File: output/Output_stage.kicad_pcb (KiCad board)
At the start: 2 copper layers, 62.9 x 27.9 mm, 16 parts, among them J1 Conn_01x03_Socket, J2 Control/LED, J3 Control/LED, Q1 BTA41, U1 MOC3041M

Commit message: Some update
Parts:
- Q1: footprint Package_TO_SOT_THT:TO-218-3_Vertical -> PCM_Package_TO_SOT_THT_AKL:TO-218-3_Vertical
- U1: footprint Package_DIP:DIP-6_W7.62mm_Socket_LongPads -> PCM_Package_DIP_AKL:DIP-6_W7.62mm_Socket_LongPads
- moved R3 13.6 mm to (83.2, 30.9)
- moved J2 13.6 mm to (107.2, 37.6)
- moved J3 13.6 mm to (107.2, 46.6)
- moved R1 13.6 mm to (108.5, 27.9)
- moved R2 13.6 mm to (78.5, 45.1)
- moved REF3 13.6 mm to (59.7, 40.0)
- moved REF5 13.6 mm to (85.5, 44.7)
- moved REF6 13.6 mm to (85.5, 44.7)
- moved U1 13.6 mm to (96.6, 37.1)
- moved kibuzzard-64EB64A3 13.6 mm to (112.0, 39.4)
- moved J1 13.6 mm to (69.3, 46.4)
- moved Q1 13.6 mm to (63.2, 29.2)
- moved REF1 13.6 mm to (61.9, 33.3)
- moved REF2 13.6 mm to (69.3, 33.3)
- moved REF4 13.6 mm to (69.3, 40.0)
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- renumbered REF** to REF1, REF** to REF2, REF** to REF3, REF** to REF4, REF** to REF5, REF** to REF6

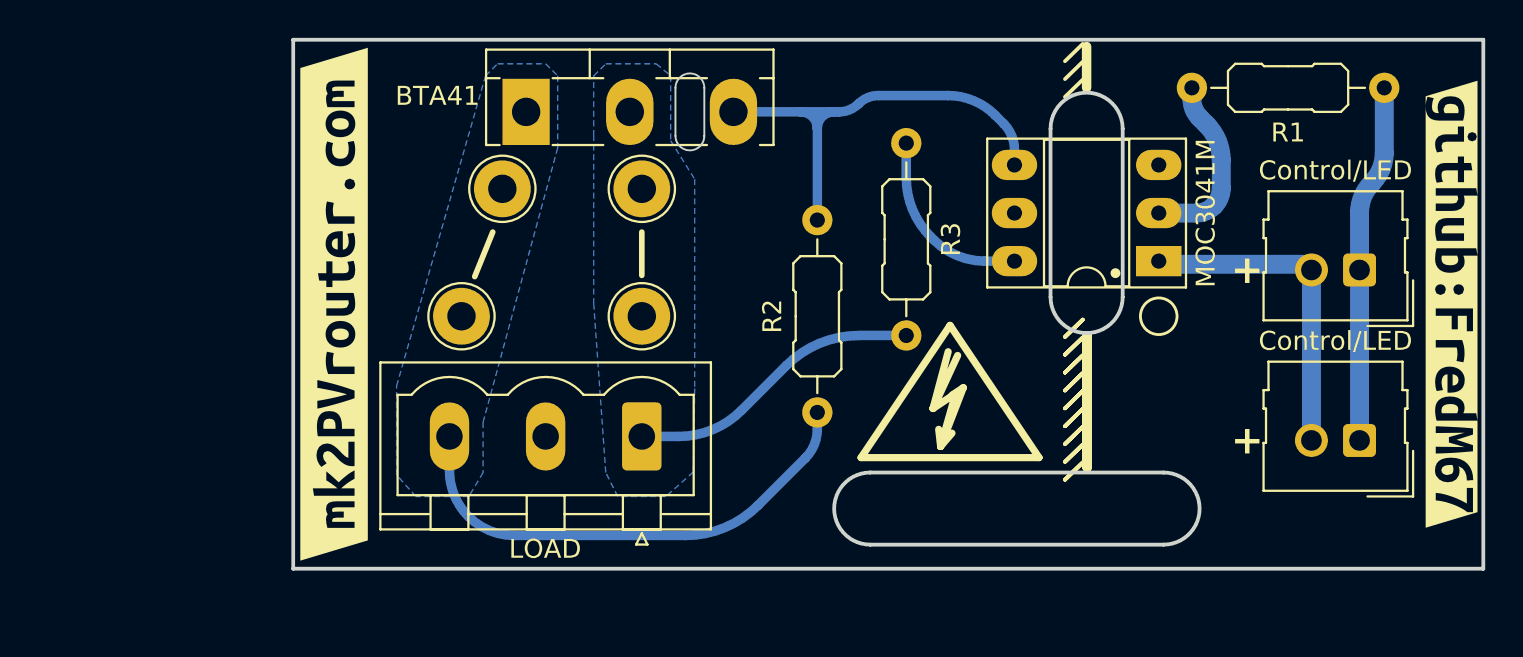
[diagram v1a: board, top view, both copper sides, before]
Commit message: Tuning output stage
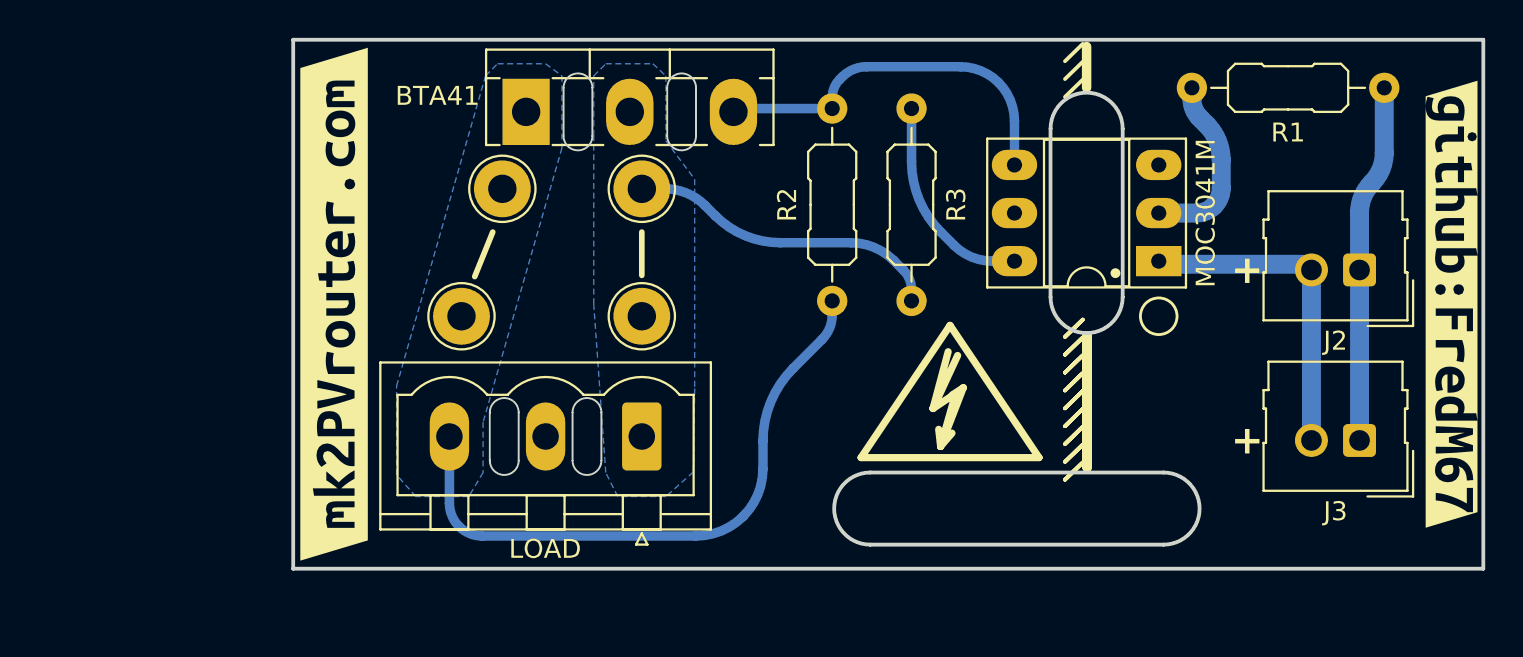
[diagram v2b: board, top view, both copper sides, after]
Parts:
- moved R2 5.94 mm to (79.3, 39.2)
- moved R3 1.85 mm to (83.5, 29.0)
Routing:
- net S/LINE: track 29.6 -> 35.3 mm
- net Net-(Q1-G): track 24.8 -> 20.1 mm
- net Net-(R3-Pad1): track 10.0 -> 11.3 mm
- net LINE: track 15.7 -> 16.8 mm
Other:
- outline, holes or cut-outs redrawn
